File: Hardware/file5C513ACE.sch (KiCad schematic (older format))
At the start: 71 parts, among them J1 GATE_2, J2 GATE_3, J3 GATE_1, Q1 MMBT3904, Q2 MMBT3904, Q3 MMBT3904, SW1 Frequency Adjust, SW10 SET_SW, SW11 FILTER_SW, SW12 FILTEREXT_SW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

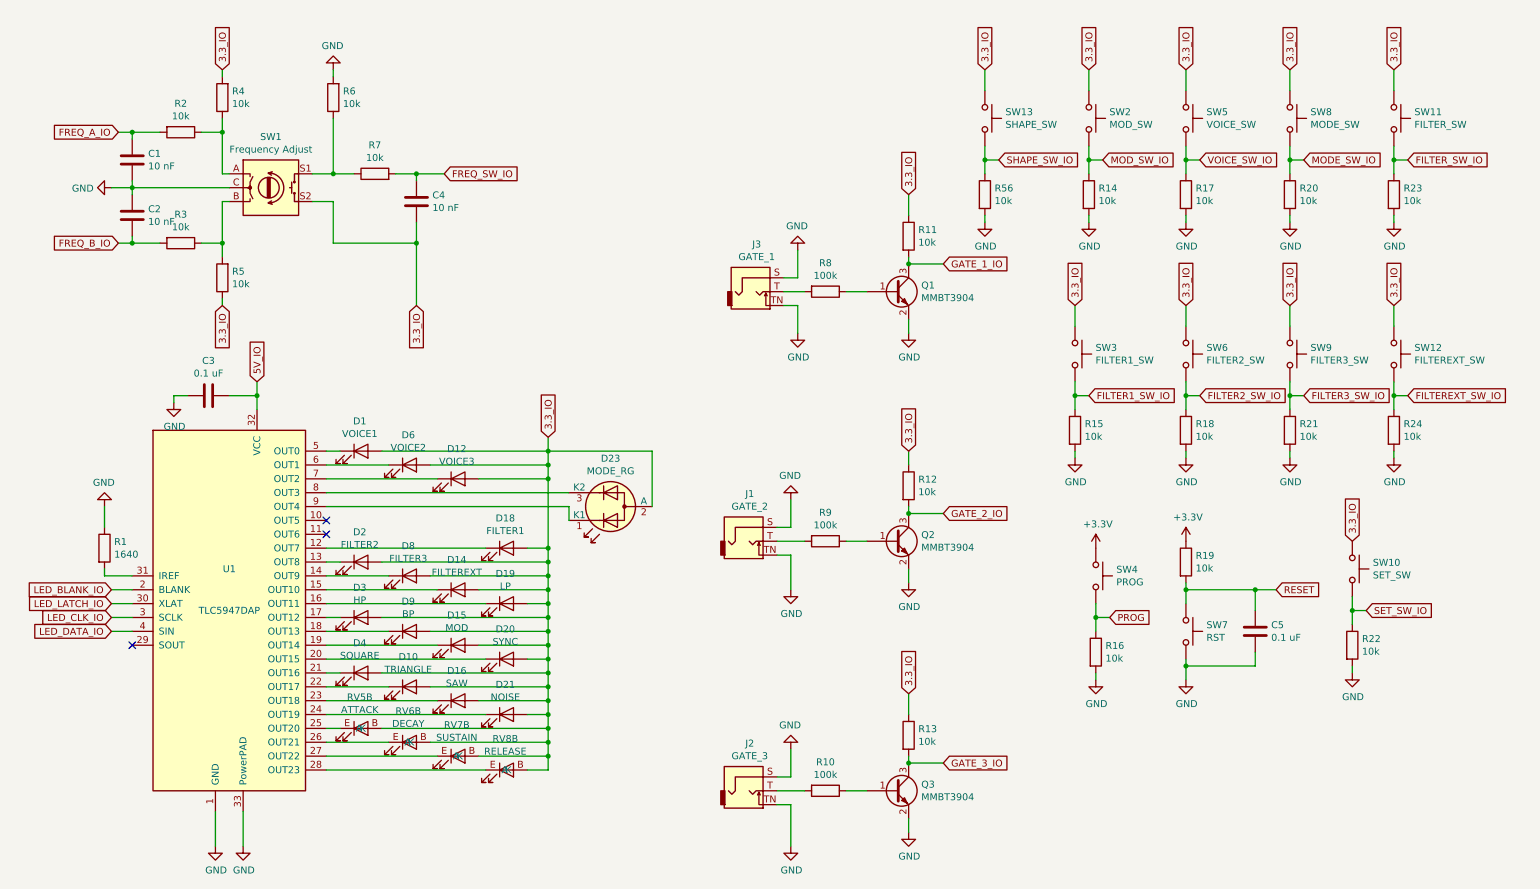
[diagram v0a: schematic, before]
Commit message: Cleaned up some traces, fixes #5
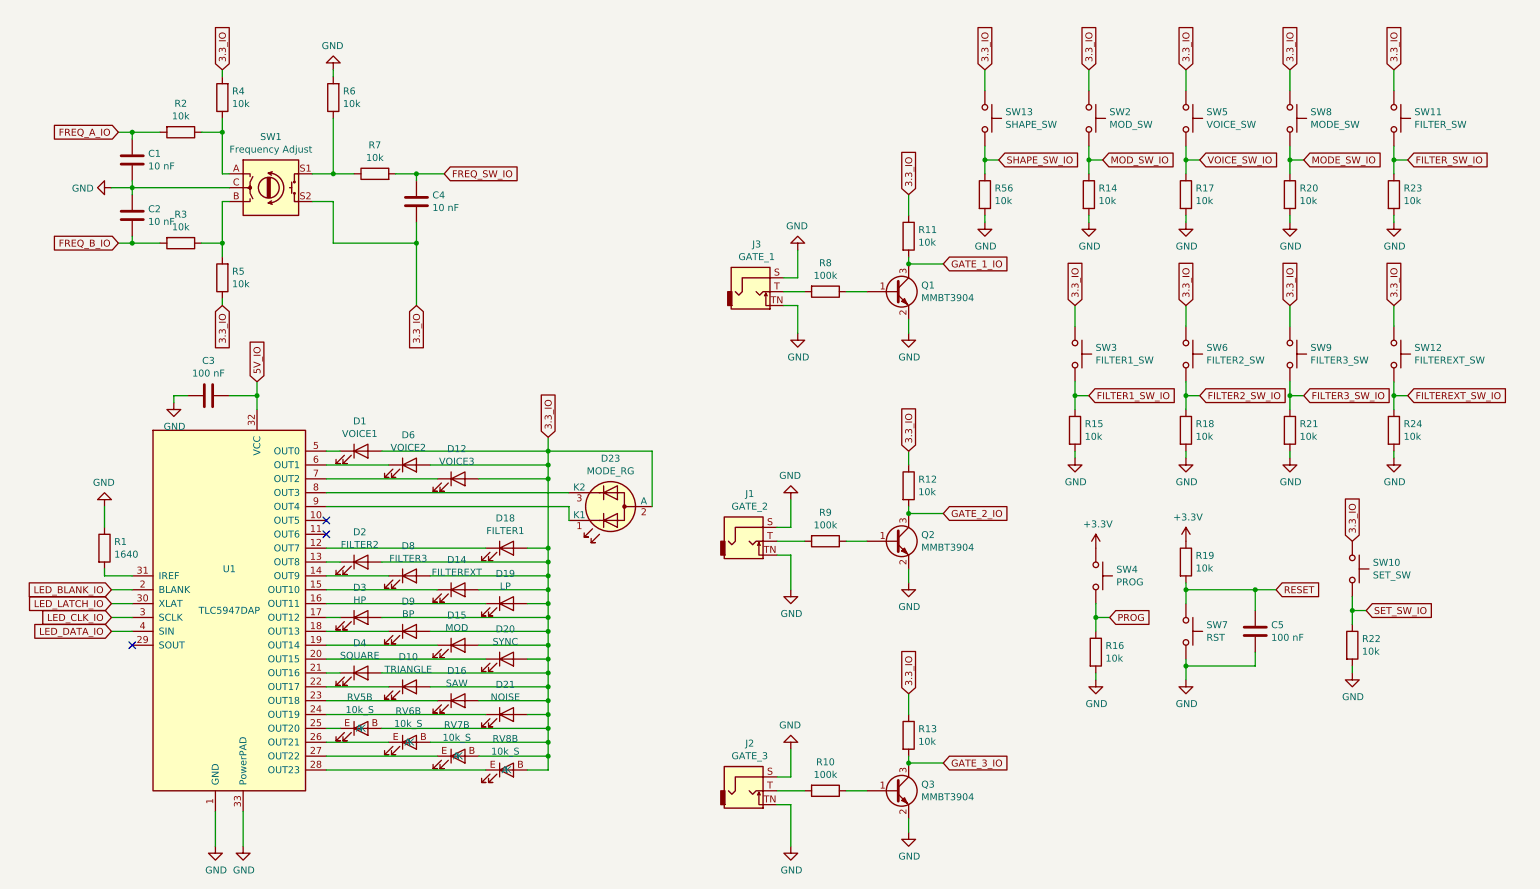
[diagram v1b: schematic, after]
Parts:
- C3, C5: value 0.1 uF -> 100 nF
- RV5: value ATTACK -> 10k_S
- RV6: value DECAY -> 10k_S
- RV7: value SUSTAIN -> 10k_S
- RV8: value RELEASE -> 10k_S
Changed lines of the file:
@@
 AR Path="/5BFD63E3/5C513ACF/5C602313" Ref="C3"  Part="1"
 F 0 "C3" V 1398 3150 50  0000 C CNN
-F 1 "0.1 uF" V 1489 3150 50  0000 C CNN
+F 1 "100 nF" V 1489 3150 50  0000 C CNN
 F 2 "Capacitor_SMD:C_0603_1608Metric" H 1688 3000 50  0001 C CNN
 F 3 "~" H 1650 3150 50  0001 C CNN
@@
 AR Path="/5BFD63E3/5C513ACF/5BF2EEEA" Ref="C5"  Part="1"
 F 0 "C5" H 9315 4896 50  0000 L CNN
-F 1 "0.1 uF" H 9315 4805 50  0000 L CNN
+F 1 "100 nF" H 9315 4805 50  0000 L CNN
 F 2 "Capacitor_SMD:C_0603_1608Metric" H 9238 4700 50  0001 C CNN
 F 3 "~" H 9200 4850 50  0001 C CNN
@@
 AR Path="/5C0B06A6" Ref="RV5"  Part="2"
 F 0 "RV5" V 2725 5341 50  0000 C CNN
-F 1 "ATTACK" V 2816 5341 50  0000 C CNN
+F 1 "10k_S" V 2816 5341 50  0000 C CNN
 F 2 "Potentiometer_THT:Potentiometer_Bourns_PTL20_Single_Slide" H 2900 5500 50  0001 C CNN
 F 3 "" H 2900 5500 50  0001 C CNN
@@
 AR Path="/5C0B06AD" Ref="RV7"  Part="2"
 F 0 "RV7" V 3425 5541 50  0000 C CNN
-F 1 "SUSTAIN" V 3516 5541 50  0000 C CNN
+F 1 "10k_S" V 3516 5541 50  0000 C CNN
 F 2 "Potentiometer_THT:Potentiometer_Bourns_PTL20_Single_Slide" H 3600 5700 50  0001 C CNN
 F 3 "" H 3600 5700 50  0001 C CNN
@@
 AR Path="/5C0B06B4" Ref="RV8"  Part="2"
 F 0 "RV8" V 3775 5641 50  0000 C CNN
-F 1 "RELEASE" V 3866 5641 50  0000 C CNN
+F 1 "10k_S" V 3866 5641 50  0000 C CNN
 F 2 "Potentiometer_THT:Potentiometer_Bourns_PTL20_Single_Slide" H 3950 5800 50  0001 C CNN
 F 3 "" H 3950 5800 50  0001 C CNN
@@
 AR Path="/5C0B06BB" Ref="RV6"  Part="2"
 F 0 "RV6" V 3075 5441 50  0000 C CNN
-F 1 "DECAY" V 3166 5441 50  0000 C CNN
+F 1 "10k_S" V 3166 5441 50  0000 C CNN
 F 2 "Potentiometer_THT:Potentiometer_Bourns_PTL20_Single_Slide" H 3250 5600 50  0001 C CNN
 F 3 "" H 3250 5600 50  0001 C CNN
